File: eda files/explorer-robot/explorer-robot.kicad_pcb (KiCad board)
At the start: 2 copper layers, 33 parts, among them J1 Conn_01x05, SW1 SW_Push, U1 RP2354B, U2 AMS1117-3.3, U3 ICM-20948, U4 TXB0108PW, Y1 ABM8-272-T3

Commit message: finish schematic for ICM-20948; requiring changes to pin assignment
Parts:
- removed C1, C2, C3: 4.7u, Capacitor_SMD:C_0402_1005Metric
- removed C10, C11, C12, C13, C14, C15, C16, C17, C18, C7, C8, C9: 100n, Capacitor_SMD:C_0201_0603Metric
- removed C19, C20: 15p, Capacitor_SMD:C_0201_0603Metric
- removed C4, C5: 10u, Capacitor_SMD:C_0201_0603Metric
- removed C6: 22u, Capacitor_Tantalum_SMD:CP_EIA-3216-18_Kemet-A
- removed J1: Conn_01x05, Connector_JST:JST_SH_BM03B-SRSS-TB_1x03-1MP_P1.00mm_Vertical
- removed L1: 3.3u, rp235xb:abracon_aota-b201610s3r3-101-t
- removed R1: 33, Resistor_SMD:R_01005_0402Metric
- removed R2: 1K, Resistor_SMD:R_0603_1608Metric
- removed R3: 1K, Resistor_SMD:R_01005_0402Metric
- removed SW1: SW_Push, Button_Switch_SMD:SW_SPST_TS-1088-xR020
- removed TP1, TP2: TestPoint_2Pole, TestPoint:TestPoint_2Pads_Pitch5.08mm_Drill1.3mm
- removed U1: RP2354B, rp235xb:rpi_rp2350b_vias
- removed U2: AMS1117-3.3, Package_TO_SOT_SMD:SOT-223-3_TabPin2
- removed U3: ICM-20948, Sensor_Motion:InvenSense_QFN-24_3x3mm_P0.4mm
- removed U4: TXB0108PW, Package_SO:TSSOP-20_4.4x6.5mm_P0.65mm
- removed Y1: ABM8-272-T3, Crystal:Crystal_SMD_Abracon_ABM8AIG-4Pin_3.2x2.5mm
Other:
- copper layers 2 -> 4

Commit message: Update AI camera branch to 5V and document schematic
- ADR-0027 supersedes ADR-0025: AI camera input is 5V, not 3.3V
- Move U9 VIN and C55 back to +5V in aicam.kicad_sch
- Update CONTEXT.md branch descriptions and ADR cross-references
- Record ICM-20948 placement status and corrected battery divider ratio
- Adjust battery_charge_read for 33k/10k divider (0.2326 ratio)
- Enable sheet component classes; refresh netlist and PCB footprints
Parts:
- added C1: 4.7u, Capacitor_SMD:C_0402_1005Metric, F.Cu at (17.3, 88.1)
- added C10: 100n, Capacitor_SMD:C_0603_1608Metric, F.Cu at (23.1, 79.5)
- added C11: 100n, Capacitor_SMD:C_0603_1608Metric, F.Cu at (27.1, 66.9)
- added C12: 100n, Capacitor_SMD:C_0603_1608Metric, F.Cu at (27.1, 69.4)
- added C13: 100n, Capacitor_SMD:C_0603_1608Metric, F.Cu at (27.1, 71.9)
- added C14: 100n, Capacitor_SMD:C_0603_1608Metric, F.Cu at (27.1, 74.4)
- added C15: 100n, Capacitor_SMD:C_0603_1608Metric, F.Cu at (27.1, 76.9)
- added C16: 100n, Capacitor_SMD:C_0603_1608Metric, F.Cu at (27.1, 79.5)
- added C17: 100n, Capacitor_SMD:C_0603_1608Metric, F.Cu at (31.1, 66.9)
- added C18: 100n, Capacitor_SMD:C_0603_1608Metric, F.Cu at (31.1, 69.4)
- added C19: 15p, Capacitor_SMD:C_0603_1608Metric, F.Cu at (31.1, 71.9)
- added C2: 4.7u, Capacitor_SMD:C_0402_1005Metric, F.Cu at (17.3, 90.0)
- added C20: 15p, Capacitor_SMD:C_0603_1608Metric, F.Cu at (31.1, 74.4)
- added C21: 100n, Capacitor_SMD:C_0603_1608Metric, F.Cu at (63.1, 101.5)
- added C22: 10u, Capacitor_SMD:C_0603_1608Metric, F.Cu at (63.1, 104.0)
- added C23: 10u, Capacitor_SMD:C_0603_1608Metric, F.Cu at (63.1, 106.5)
- added C24: 22u, Capacitor_Tantalum_SMD:CP_EIA-3216-18_Kemet-A, F.Cu at (77.8, 117.0)
- added C25: 100n, Capacitor_SMD:C_0603_1608Metric, F.Cu at (63.1, 109.0)
- added C26: 100n, Capacitor_SMD:C_0603_1608Metric, F.Cu at (63.1, 111.5)
- added C27: 100n, Capacitor_SMD:C_0603_1608Metric, F.Cu at (63.1, 114.0)
- added C28: 100n, Capacitor_SMD:C_0603_1608Metric, F.Cu at (63.1, 116.5)
- added C3: 4.7u, Capacitor_SMD:C_0402_1005Metric, F.Cu at (17.3, 92.0)
- added C31: 100n, Capacitor_SMD:C_0603_1608Metric, F.Cu at (250.4, 149.9)
- added C32: 10n, Capacitor_SMD:C_0603_1608Metric, F.Cu at (250.4, 152.4)
- added C33: 1u, Capacitor_SMD:C_0603_1608Metric, F.Cu at (250.4, 154.9)
- added C34: 10n, Capacitor_SMD:C_0603_1608Metric, F.Cu at (250.4, 157.4)
- added C35: 10u, Capacitor_SMD:C_0805_2012Metric, F.Cu at (129.5, 99.2)
- added C36: 1u, Capacitor_SMD:C_0603_1608Metric, F.Cu at (254.4, 149.9)
- added C37: 100n, Capacitor_SMD:C_0603_1608Metric, F.Cu at (254.4, 152.4)
- added C38: 10u, Capacitor_SMD:C_0805_2012Metric, F.Cu at (126.2, 99.2)
- added C39: 10u, Capacitor_SMD:C_0805_2012Metric, F.Cu at (123.0, 99.2)
- added C4: 10u, Capacitor_SMD:C_0603_1608Metric, F.Cu at (23.1, 66.9)
- added C40: 10u, Capacitor_SMD:C_0805_2012Metric, F.Cu at (74.5, 73.7)
- added C41: 100n, Capacitor_SMD:C_0603_1608Metric, F.Cu at (254.4, 154.9)
- added C42: 1u, Capacitor_SMD:C_0603_1608Metric, F.Cu at (254.4, 157.4)
- added C43: 100n, Capacitor_SMD:C_0603_1608Metric, F.Cu at (258.4, 149.9)
- added C44: 1u, Capacitor_SMD:C_0603_1608Metric, F.Cu at (258.4, 152.4)
- added C45: 100n, Capacitor_SMD:C_0603_1608Metric, F.Cu at (168.8, 67.7)
- added C46: 1u, Capacitor_SMD:C_0603_1608Metric, F.Cu at (166.5, 67.8)
- added C47: 10n, Capacitor_SMD:C_0805_2012Metric, F.Cu at (142.0, 99.2)
- added C48: 220u, Capacitor_SMD:CP_Elec_6.3x7.7, F.Cu at (167.2, 103.0)
- added C49: 220u, Capacitor_SMD:CP_Elec_6.3x7.7, F.Cu at (269.6, 132.5)
- added C5: 10u, Capacitor_SMD:C_0603_1608Metric, F.Cu at (23.1, 69.4)
- added C50: 220u, Capacitor_SMD:CP_Elec_6.3x7.7, F.Cu at (202.8, 70.5)
- added C51: 220u, Capacitor_SMD:CP_Elec_6.3x7.7, F.Cu at (161.5, 69.5)
- added C52: 1u, Capacitor_SMD:C_0603_1608Metric, F.Cu at (65.1, 66.9)
- added C53: 1u, Capacitor_SMD:C_0603_1608Metric, F.Cu at (65.1, 69.4)
- added C54: 1u, Capacitor_SMD:C_0603_1608Metric, F.Cu at (65.1, 81.5)
- added C55: 1u, Capacitor_SMD:C_0603_1608Metric, F.Cu at (65.1, 84.0)
- added C56: 1u, Capacitor_SMD:C_0603_1608Metric, F.Cu at (63.1, 121.8)
- added C57: 1u, Capacitor_SMD:C_0603_1608Metric, F.Cu at (63.1, 124.3)
- added C58: 1u, Capacitor_SMD:C_0603_1608Metric, F.Cu at (41.2, 64.8)
- added C59: 1u, Capacitor_SMD:C_0603_1608Metric, F.Cu at (37.1, 76.0)
- added C6: 22u, Capacitor_Tantalum_SMD:CP_EIA-3216-18_Kemet-A, F.Cu at (24.0, 94.1)
- added C60: 10u, Capacitor_SMD:C_0805_2012Metric, F.Cu at (74.5, 88.3)
- added C61: 10u, Capacitor_SMD:C_0805_2012Metric, F.Cu at (67.3, 135.1)
- added C62: 10u, Capacitor_SMD:C_0805_2012Metric, F.Cu at (58.4, 67.2)
- added C63: 10u, Capacitor_SMD:C_0805_2012Metric, F.Cu at (48.9, 146.1)
- added C64: 100n, Capacitor_SMD:C_0603_1608Metric, F.Cu at (48.7, 133.3)
- added C65: 10u, Capacitor_SMD:C_0805_2012Metric, F.Cu at (48.9, 149.1)
- added C66: 100n, Capacitor_SMD:C_0603_1608Metric, F.Cu at (48.7, 135.8)
- added C7: 100n, Capacitor_SMD:C_0603_1608Metric, F.Cu at (23.1, 71.9)
- added C8: 100n, Capacitor_SMD:C_0603_1608Metric, F.Cu at (23.1, 74.4)
- added C9: 100n, Capacitor_SMD:C_0603_1608Metric, F.Cu at (23.1, 76.9)
- added D1: D_TVS, Diode_SMD:D_SMA, F.Cu at (264.5, 150.9)
- added D2: D_TVS, Diode_SMD:D_SMA, F.Cu at (264.5, 155.5)
- added D3: D_TVS, Diode_SMD:D_SMA, F.Cu at (264.5, 160.0)
- added D4: D_TVS, Diode_SMD:D_SMA, F.Cu at (177.5, 69.2)
- added D5: 3A 40V, Diode_SMD:D_SMA, F.Cu at (146.7, 101.8)
- added H1: MountingHole_Pad, MountingHole:MountingHole_3.2mm_M3_Pad_Via, F.Cu at (102.2, 51.0)
- added H2: MountingHole_Pad, MountingHole:MountingHole_3.2mm_M3_Pad_Via, F.Cu at (183.8, 51.1)
- added H3: MountingHole_Pad, MountingHole:MountingHole_3.2mm_M3_Pad_Via, F.Cu at (184.0, 132.9)
- added H4: MountingHole_Pad, MountingHole:MountingHole_3.2mm_M3_Pad_Via, F.Cu at (102.1, 132.9)
- added J1: DBG, Connector_JST:JST_SH_BM03B-SRSS-TB_1x03-1MP_P1.00mm_Vertical, F.Cu at (7.00, 92.8)
- added J10: EXP.DATA, Connector_JST:JST_PH_B5B-PH-K_1x05_P2.00mm_Vertical, F.Cu at (160.5, 50.5)
- added J11: PANEL.BUS, Connector_JST:JST_PH_B5B-PH-K_1x05_P2.00mm_Vertical, F.Cu at (137.2, 50.8)
- added J12: PANEL.CTRL, Connector_JST:JST_PH_B6B-PH-K_1x06_P2.00mm_Vertical, F.Cu at (121.2, 50.8)
- added J13: RF.FRONT, Connector_JST:JST_PH_B6B-PH-K_1x06_P2.00mm_Vertical, F.Cu at (119.0, 133.1)
- added J14: RF.REAR, Connector_JST:JST_PH_B6B-PH-K_1x06_P2.00mm_Vertical, F.Cu at (135.0, 133.0)
- added J2: MAL, Connector_JST:JST_PH_B6B-PH-K_1x06_P2.00mm_Vertical, F.Cu at (184.0, 84.0)
- added J3: MBR, Connector_JST:JST_PH_B6B-PH-K_1x06_P2.00mm_Vertical, F.Cu at (184.0, 100.2)
- added J4: BAT, Connector_JST:JST_XH_B2B-XH-A_1x02_P2.50mm_Vertical, F.Cu at (183.5, 68.0)
- added J5: LED, Connector_JST:JST_PH_B4B-PH-K_1x04_P2.00mm_Vertical, F.Cu at (147.0, 133.0)
- added J7: LID, Connector_JST:JST_PH_B4B-PH-K_1x04_P2.00mm_Vertical, F.Cu at (109.3, 50.8)
- added J8: AI.CAM, Connector_JST:JST_PH_B4B-PH-K_1x04_P2.00mm_Vertical, F.Cu at (101.8, 64.2)
- added J9: EXP.PWR, Connector_JST:JST_PH_B2B-PH-K_1x02_P2.00mm_Vertical, F.Cu at (174.8, 50.5)
- added L1: 3.3u, rp235xb:abracon_aota-b201610s3r3-101-t, F.Cu at (0.19, 96.8)
- added L2: 15u, Inductor_SMD:L_AVX_LMLP07A7, F.Cu at (155.2, 100.0)
- added Q1: Q_PMOS_GSD, Package_TO_SOT_SMD:SOT-23, F.Cu at (172.0, 69.6)
- added R1: 33, Resistor_SMD:R_0402_1005Metric, F.Cu at (17.3, 94.0)
- added R10: 220, Resistor_SMD:R_0603_1608Metric, F.Cu at (0.14, 143.9)
- added R11: 220, Resistor_SMD:R_0603_1608Metric, F.Cu at (0.14, 146.4)
- added R12: 330, Resistor_SMD:R_0603_1608Metric, F.Cu at (0.14, 148.9)
- added R13: 10K, Resistor_SMD:R_0603_1608Metric, F.Cu at (220.2, 77.2)
- added R14: 20K, Resistor_SMD:R_0603_1608Metric, F.Cu at (225.2, 75.7)
- added R15: 100, Resistor_SMD:R_0603_1608Metric, F.Cu at (65.1, 71.9)
- added R16: 100, Resistor_SMD:R_0603_1608Metric, F.Cu at (65.1, 74.4)
- added R17: 100, Resistor_SMD:R_0603_1608Metric, F.Cu at (65.1, 76.9)
- added R18: 100, Resistor_SMD:R_0603_1608Metric, F.Cu at (65.1, 86.5)
- added R19: 100, Resistor_SMD:R_0603_1608Metric, F.Cu at (65.1, 89.0)
- added R2: 1K, Resistor_SMD:R_0603_1608Metric, F.Cu at (31.1, 76.9)
- added R20: 100, Resistor_SMD:R_0603_1608Metric, F.Cu at (65.1, 91.5)
- added R21: 100, Resistor_SMD:R_0603_1608Metric, F.Cu at (63.1, 126.8)
- added R22: 100, Resistor_SMD:R_0603_1608Metric, F.Cu at (63.1, 129.3)
- added R23: 100, Resistor_SMD:R_0603_1608Metric, F.Cu at (63.1, 131.8)
- added R24: 1k, Resistor_SMD:R_0603_1608Metric, F.Cu at (63.1, 134.3)
- added R25: 1k, Resistor_SMD:R_0603_1608Metric, F.Cu at (63.1, 136.9)
- added R26: 1k, Resistor_SMD:R_0603_1608Metric, F.Cu at (63.1, 139.4)
- added R27: 33, Resistor_SMD:R_0603_1608Metric, F.Cu at (37.1, 78.5)
- added R28: 33, Resistor_SMD:R_0603_1608Metric, F.Cu at (37.1, 81.0)
- added R29: 33, Resistor_SMD:R_0603_1608Metric, F.Cu at (41.1, 73.5)
- added R3: 1K, Resistor_SMD:R_0402_1005Metric, F.Cu at (17.3, 96.0)
- added R30: 100, Resistor_SMD:R_0603_1608Metric, F.Cu at (41.1, 76.0)
- added R31: 100, Resistor_SMD:R_0603_1608Metric, F.Cu at (41.1, 78.5)
- added R32: 100, Resistor_SMD:R_0603_1608Metric, F.Cu at (41.1, 81.0)
- added R33: 100, Resistor_SMD:R_0603_1608Metric, F.Cu at (45.1, 73.5)
- added R34: 100, Resistor_SMD:R_0603_1608Metric, F.Cu at (45.1, 76.0)
- added R35: 1k, Resistor_SMD:R_0603_1608Metric, F.Cu at (45.1, 78.5)
- added R36: 100, Resistor_SMD:R_0603_1608Metric, F.Cu at (45.1, 81.0)
- added R37: 33, Resistor_SMD:R_0603_1608Metric, F.Cu at (48.7, 138.3)
- added R38: 33, Resistor_SMD:R_0603_1608Metric, F.Cu at (48.7, 140.9)
- added R39: 4k7, Resistor_SMD:R_0603_1608Metric, F.Cu at (48.7, 143.4)
- added R4: 100K, Resistor_SMD:R_0402_1005Metric, F.Cu at (80.3, 106.1)
- added R40: 4k7, Resistor_SMD:R_0603_1608Metric, F.Cu at (52.7, 133.3)
- added R41: 33, Resistor_SMD:R_0603_1608Metric, F.Cu at (52.7, 135.8)
- added R42: 33, Resistor_SMD:R_0603_1608Metric, F.Cu at (52.7, 138.3)
- added R43: 4k7, Resistor_SMD:R_0603_1608Metric, F.Cu at (52.7, 140.9)
- added R44: 4k7, Resistor_SMD:R_0603_1608Metric, F.Cu at (52.7, 143.4)
- added R45: 150, Resistor_SMD:R_0603_1608Metric, F.Cu at (44.5, 91.0)
- added R5: 2.2K, Resistor_SMD:R_0603_1608Metric, F.Cu at (258.4, 154.9)
- added R6: 100K, Resistor_SMD:R_0402_1005Metric, F.Cu at (174.5, 66.7)
- added R7: 2.2K, Resistor_SMD:R_0603_1608Metric, F.Cu at (258.4, 157.4)
- added R8: 10K, Resistor_SMD:R_0603_1608Metric, F.Cu at (162.5, 97.8)
- added R9: 3K3, Resistor_SMD:R_0603_1608Metric, F.Cu at (162.5, 93.4)
- added SW1: SW_Push, Button_Switch_SMD:SW_SPST_TS-1088-xR020, F.Cu at (12.0, 99.8)
- added TP1: T.LR.5V, Connector_PinHeader_2.54mm:PinHeader_1x02_P2.54mm_Vertical, F.Cu at (0.43, 67.9)
- added TP10: T.MOT.B, Connector_PinHeader_2.54mm:PinHeader_1x02_P2.54mm_Vertical, F.Cu at (250.7, 143.8)
- added TP11: T.MOT.A, Connector_PinHeader_2.54mm:PinHeader_1x02_P2.54mm_Vertical, F.Cu at (255.3, 143.8)
- added TP12: T.PWR.BAT, Connector_PinHeader_2.54mm:PinHeader_1x02_P2.54mm_Vertical, F.Cu at (214.1, 68.5)
- added TP13: T.PWR.5V, Connector_PinHeader_2.54mm:PinHeader_1x02_P2.54mm_Vertical, F.Cu at (221.0, 66.7)
- added TP14: T.SPI0.CLK, Connector_PinHeader_2.54mm:PinHeader_1x02_P2.54mm_Vertical, F.Cu at (9.61, 67.9)
- added TP15: T.SPI0.MOSI, Connector_PinHeader_2.54mm:PinHeader_1x02_P2.54mm_Vertical, F.Cu at (14.2, 67.9)
- added TP16: T.SPI0.MISO, Connector_PinHeader_2.54mm:PinHeader_1x02_P2.54mm_Vertical, F.Cu at (18.8, 67.9)
- added TP17: T.SPI1.CLK, Connector_PinHeader_2.54mm:PinHeader_1x02_P2.54mm_Vertical, F.Cu at (0.43, 75.1)
- added TP18: T.SPI1.MOSI, Connector_PinHeader_2.54mm:PinHeader_1x02_P2.54mm_Vertical, F.Cu at (5.02, 75.1)
- added TP19: T.SPI1.MISO, Connector_PinHeader_2.54mm:PinHeader_1x02_P2.54mm_Vertical, F.Cu at (9.61, 75.1)
- added TP2: T.LR.3V3, Connector_PinHeader_2.54mm:PinHeader_1x02_P2.54mm_Vertical, F.Cu at (5.02, 67.9)
- added TP20: T.TCH.PEN, Connector_PinHeader_2.54mm:PinHeader_1x02_P2.54mm_Vertical, F.Cu at (49.4, 74.5)
- added TP21: T.TCH.CS, Connector_PinHeader_2.54mm:PinHeader_1x02_P2.54mm_Vertical, F.Cu at (54.0, 74.5)
- added TP22: T.LCD.CS, Connector_PinHeader_2.54mm:PinHeader_1x02_P2.54mm_Vertical, F.Cu at (58.6, 74.5)
- added TP23: T.PWR.1V1, Connector_PinHeader_2.54mm:PinHeader_1x02_P2.54mm_Vertical, F.Cu at (14.2, 75.1)
- added TP24: T.MOT.ENC.A, Connector_PinHeader_2.54mm:PinHeader_1x02_P2.54mm_Vertical, F.Cu at (259.9, 143.8)
- added TP25: T.MOT.ENC.B, Connector_PinHeader_2.54mm:PinHeader_1x02_P2.54mm_Vertical, F.Cu at (264.5, 143.8)
- added TP26: T.I2C1.SDA, Connector_PinHeader_2.54mm:PinHeader_1x02_P2.54mm_Vertical, F.Cu at (18.8, 75.1)
- added TP27: T.I2C1.SCL, Connector_PinHeader_2.54mm:PinHeader_1x02_P2.54mm_Vertical, F.Cu at (0.43, 82.2)
- added TP28: T.I2C0.SDA, Connector_PinHeader_2.54mm:PinHeader_1x02_P2.54mm_Vertical, F.Cu at (5.02, 82.2)
- added TP29: T.I2C0.SCL, Connector_PinHeader_2.54mm:PinHeader_1x02_P2.54mm_Vertical, F.Cu at (9.61, 82.2)
- added TP4: T.LR.1V8, Connector_PinHeader_2.54mm:PinHeader_1x02_P2.54mm_Vertical, F.Cu at (67.4, 102.5)
- added TP8: T.IMU.CS, Connector_PinHeader_2.54mm:PinHeader_1x02_P2.54mm_Vertical, F.Cu at (72.0, 102.5)
- added TP9: T.IMU.INT, Connector_PinHeader_2.54mm:PinHeader_1x02_P2.54mm_Vertical, F.Cu at (76.6, 102.5)
- added U1: RP2354B, rp235xb:rpi_rp2350b_vias, F.Cu at (27.1, 86.7)
- added U10: TPS22917DBV, Package_TO_SOT_SMD:SOT-23-6, F.Cu at (75.6, 129.5)
- added U11: TPS22917DBV, Package_TO_SOT_SMD:SOT-23-6, F.Cu at (48.9, 64.7)
- added U2: AMS1117-3.3, Package_TO_SOT_SMD:SOT-223-3_TabPin2, F.Cu at (-2.90, 105.0)
- added U3: ICM-20948, easyeda imports:QFN-24_L3.0-W3.0-P0.40-BL-EP, F.Cu at (81.1, 102.6)
- added U4: TXB0108PW, Package_SO:TSSOP-20_4.4x6.5mm_P0.65mm, F.Cu at (79.7, 111.4)
- added U5: AMS1117-1.8, Package_TO_SOT_SMD:SOT-223-3_TabPin2, F.Cu at (51.1, 89.8)
- added U6: TB6612FNG, Package_SO:SSOP-24_5.3x8.2mm_P0.65mm, F.Cu at (273.8, 153.7)
- added U7: TPS5430DDA, Package_SO:TI_SO-PowerPAD-8_ThermalVias, F.Cu at (135.5, 97.0)
- added U8: TPS22917DBV, Package_TO_SOT_SMD:SOT-23-6, F.Cu at (69.7, 74.6)
- added U9: TPS22917DBV, Package_TO_SOT_SMD:SOT-23-6, F.Cu at (69.7, 89.2)
- added Y1: ABM8-272-T3, easyeda imports:CRYSTAL-SMD_4P-L3.2-W2.5-BL, F.Cu at (29.5, 94.9)
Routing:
- net /Power and Battery/BAT: track 0.00 -> 12.1 mm
- net +8V: track 0.00 -> 8.94 mm
- net GND: track 0.00 -> 5.49 mm, vias 0 -> 2
- net Net-(Q1-G): track 0.00 -> 2.12 mm
- added copper zone on In1.Cu, net GND
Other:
- board outline added: 90 x 90 mm

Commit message: Rewrite ADR-0019 for L2 footprint findings
Document that the schematic uses JLC's EasyEDA footprint for the
Sunltech inductor rather than the datasheet land pattern, and update
the open items to decide whether to accept it or resize to the
datasheet geometry and sync the still-mismatched PCB instance.
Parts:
- added C29: 1n, Capacitor_SMD:C_0603_1608Metric, F.Cu at (42.5, 111.0)
- added C30: 1n, Capacitor_SMD:C_0603_1608Metric, F.Cu at (48.5, 111.0)
- added C67: 1n, Capacitor_SMD:C_0603_1608Metric, F.Cu at (42.5, 106.5)
- added C68: 1n, Capacitor_SMD:C_0603_1608Metric, F.Cu at (48.5, 106.5)
- added R46: 2K2, Resistor_SMD:R_0603_1608Metric, F.Cu at (42.5, 115.5)
- C32, C34: value 10n -> 2n2
- R14: value 20K -> 33K
- moved D1 130.3 mm to (148.8, 91.0), turned to 180 degrees
- moved C49 127.3 mm to (152.5, 82.5), turned to 90 degrees
- moved U6 126.9 mm to (159.2, 99.0), turned to -90 degrees
- moved C33 119.7 mm to (151.0, 88.2)
- moved C31 114.4 mm to (154.0, 88.2), turned to 180 degrees
- moved D2 110.0 mm to (177.0, 88.8), turned to 90 degrees
- moved C42 105.8 mm to (179.8, 82.5), turned to -90 degrees
- moved C37 105.8 mm to (159.2, 106.2), turned to 90 degrees
- moved D3 103.4 mm to (177.0, 105.0), turned to 90 degrees
- moved C36 103.4 mm to (160.7, 106.2), turned to 90 degrees
- moved TP24 102.4 mm to (169.8, 95.2), turned to 90 degrees
- moved C41 101.8 mm to (179.8, 85.7), turned to 90 degrees
- moved TP11 101.5 mm to (171.0, 87.2)
- moved R5 100.2 mm to (178.5, 94.5)
- moved TP25 100.0 mm to (169.7, 111.8), turned to 90 degrees
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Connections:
- C25 pad 2: +3.3V -> +1V8
- C55 pad 2: +3.3V -> +5V
- U10 pad 4: unconnected-(U10-CT-Pad4) -> Net-(U10-CT)
- U11 pad 4: unconnected-(U11-CT-Pad4) -> Net-(U11-CT)
- U3 pad 13: +3.3V -> +1V8
- U4 pad 1: unconnected-(U4-A1-Pad1) -> GND
- U4 pad 17: unconnected-(U4-B3-Pad17) -> GND
- U4 pad 18: unconnected-(U4-B2-Pad18) -> GND
- U4 pad 20: unconnected-(U4-B1-Pad20) -> GND
- U4 pad 3: unconnected-(U4-A2-Pad3) -> GND
- U4 pad 4: unconnected-(U4-A3-Pad4) -> GND
- U8 pad 4: unconnected-(U8-CT-Pad4) -> Net-(U8-CT)
- U9 pad 1: +3.3V -> +5V
- U9 pad 4: unconnected-(U9-CT-Pad4) -> Net-(U9-CT)
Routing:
- net +8V: track 8.94 -> 102.1 mm
- net GND: track 5.49 -> 47.9 mm, vias 2 -> 32
- net /TB6612FNG and encoders/B01: track 0.00 -> 37.9 mm
- net /TB6612FNG and encoders/A01: track 0.00 -> 37.1 mm
- net /TB6612FNG and encoders/B02: track 0.00 -> 36.1 mm, vias 0 -> 2
- net /TB6612FNG and encoders/A02: track 0.00 -> 31.9 mm, vias 0 -> 2
- net +5V: track 0.00 -> 30.6 mm, vias 0 -> 3
- net /TB6612FNG and encoders/MOT.B.R.ENC.A: track 0.00 -> 15.1 mm
- net Net-(U7-VSENSE): track 0.00 -> 14.7 mm
- net Net-(D5-K): track 0.00 -> 10.3 mm
- net Net-(J2-Pin_3): track 0.00 -> 9.12 mm, vias 0 -> 1
- net /TB6612FNG and encoders/MOT.A.L.ENC.A: track 0.00 -> 8.65 mm
- net +3.3V: track 0.00 -> 5.75 mm, vias 0 -> 6
- net /Power and Battery/BATT_ADC: track 0.00 -> 4.77 mm
- net Net-(U7-BOOT): track 0.00 -> 2.77 mm
- added copper zone on In2.Cu, net +3.3V
- added copper zone on In2.Cu, net +5V

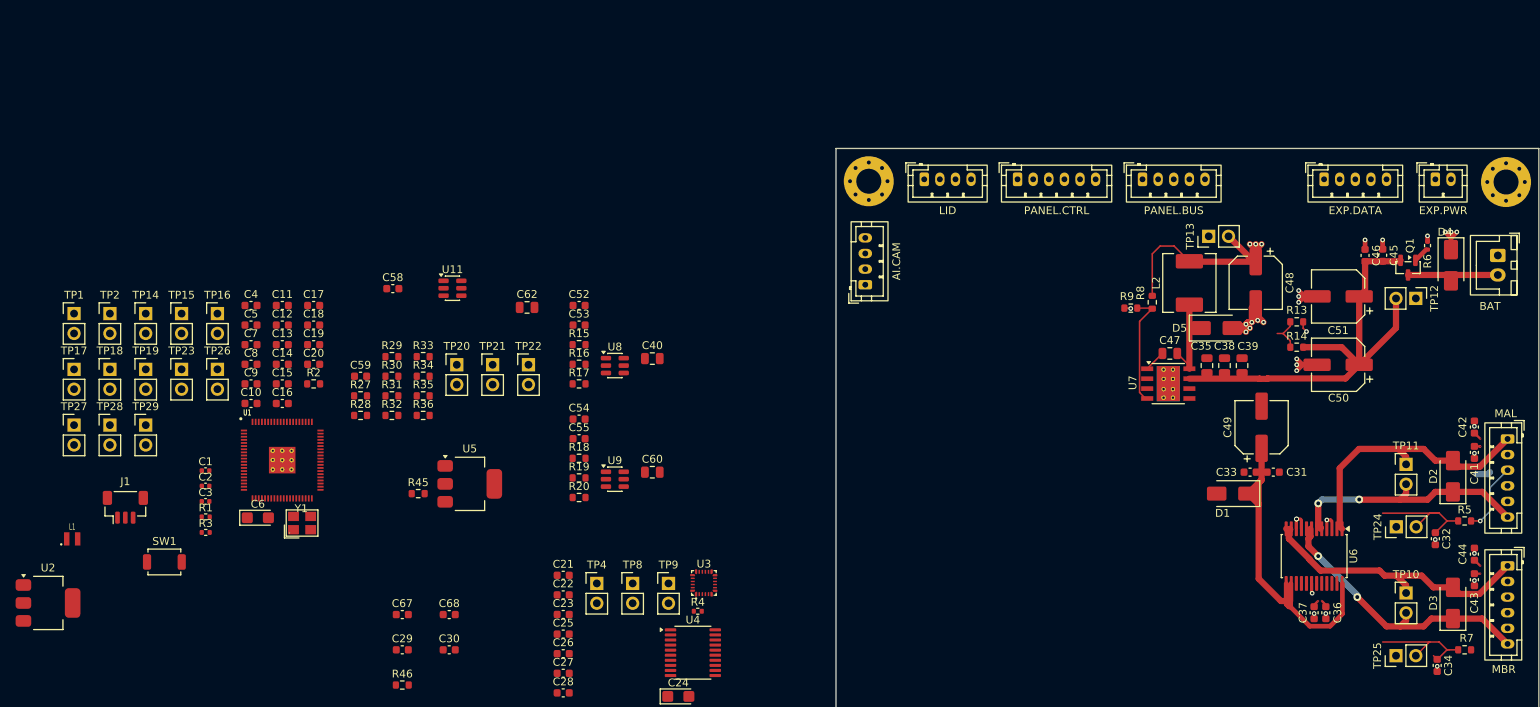
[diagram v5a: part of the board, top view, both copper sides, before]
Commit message: Fix DRC violations and tune design rules for JLCPCB
Add local edits to the generated DRC file: exclude custom pads from
the SMD pad size rule and relax pad-to-pad clearance to 0.127 mm to
accommodate U3's 0.4 mm-pitch QFN pads. Update board layout and
netclass/via settings, and add a DRC exclusion for a footprint mismatch.
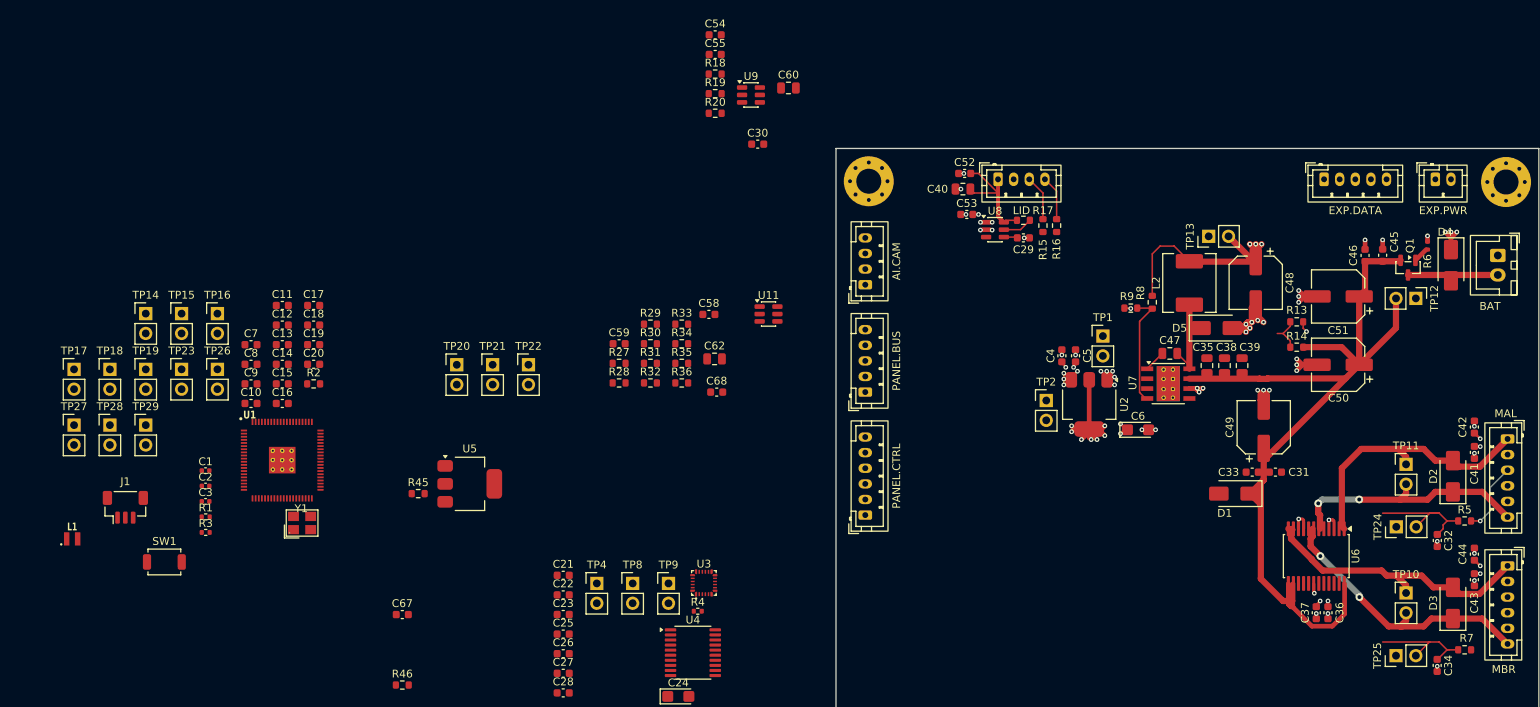
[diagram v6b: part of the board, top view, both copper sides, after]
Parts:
- moved U2 135.7 mm to (130.4, 79.6), turned to -90 degrees
- moved TP1 131.8 mm to (132.2, 70.8)
- moved TP2 120.4 mm to (124.9, 79.1)
- moved C6 113.3 mm to (136.7, 82.8)
- moved C5 105.7 mm to (128.7, 73.3), turned to 90 degrees
- moved C4 104.0 mm to (126.9, 73.3), turned to 90 degrees
- moved C29 95.4 mm to (122.0, 58.2)
- moved C30 75.8 mm to (88.0, 46.2)
- moved R16 63.7 mm to (126.2, 56.7), turned to 90 degrees
- moved R15 61.3 mm to (124.5, 56.7), turned to 90 degrees
- moved R17 60.6 mm to (122.0, 56.0)
- moved C60 52.2 mm to (91.9, 39.1)
- moved R18 52.2 mm to (82.5, 37.3)
- moved C55 52.2 mm to (82.5, 34.8)
- moved R19 52.2 mm to (82.5, 39.8)
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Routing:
- net GND: track 47.9 -> 72.9 mm, vias 32 -> 51
- net +3.3V: track 5.75 -> 28.1 mm, vias 6 -> 15
- net Net-(J7-Pin_1): track 0.00 -> 15.9 mm
- net +8V: track 102.1 -> 117.1 mm
- net +5V: track 30.6 -> 41.6 mm, vias 3 -> 13
- net Net-(J7-Pin_3): track 0.00 -> 5.82 mm
- net Net-(J7-Pin_4): track 0.00 -> 5.72 mm
- net Net-(U8-QOD): track 0.00 -> 3.82 mm
- net /TB6612FNG and encoders/A01: track 37.1 -> 35.2 mm
- net Net-(U8-CT): track 0.00 -> 1.77 mm
- net /TB6612FNG and encoders/MOT.B.R.ENC.A: track 15.1 -> 14.4 mm
